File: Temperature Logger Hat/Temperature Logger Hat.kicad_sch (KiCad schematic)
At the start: 18 parts, among them J1 GPIO, J2 SPI, J3 1-wire, J4 Jumper_Mode, SW1 SW_Power_Off, SW2 SW_Mode2, U1 CAT24C256

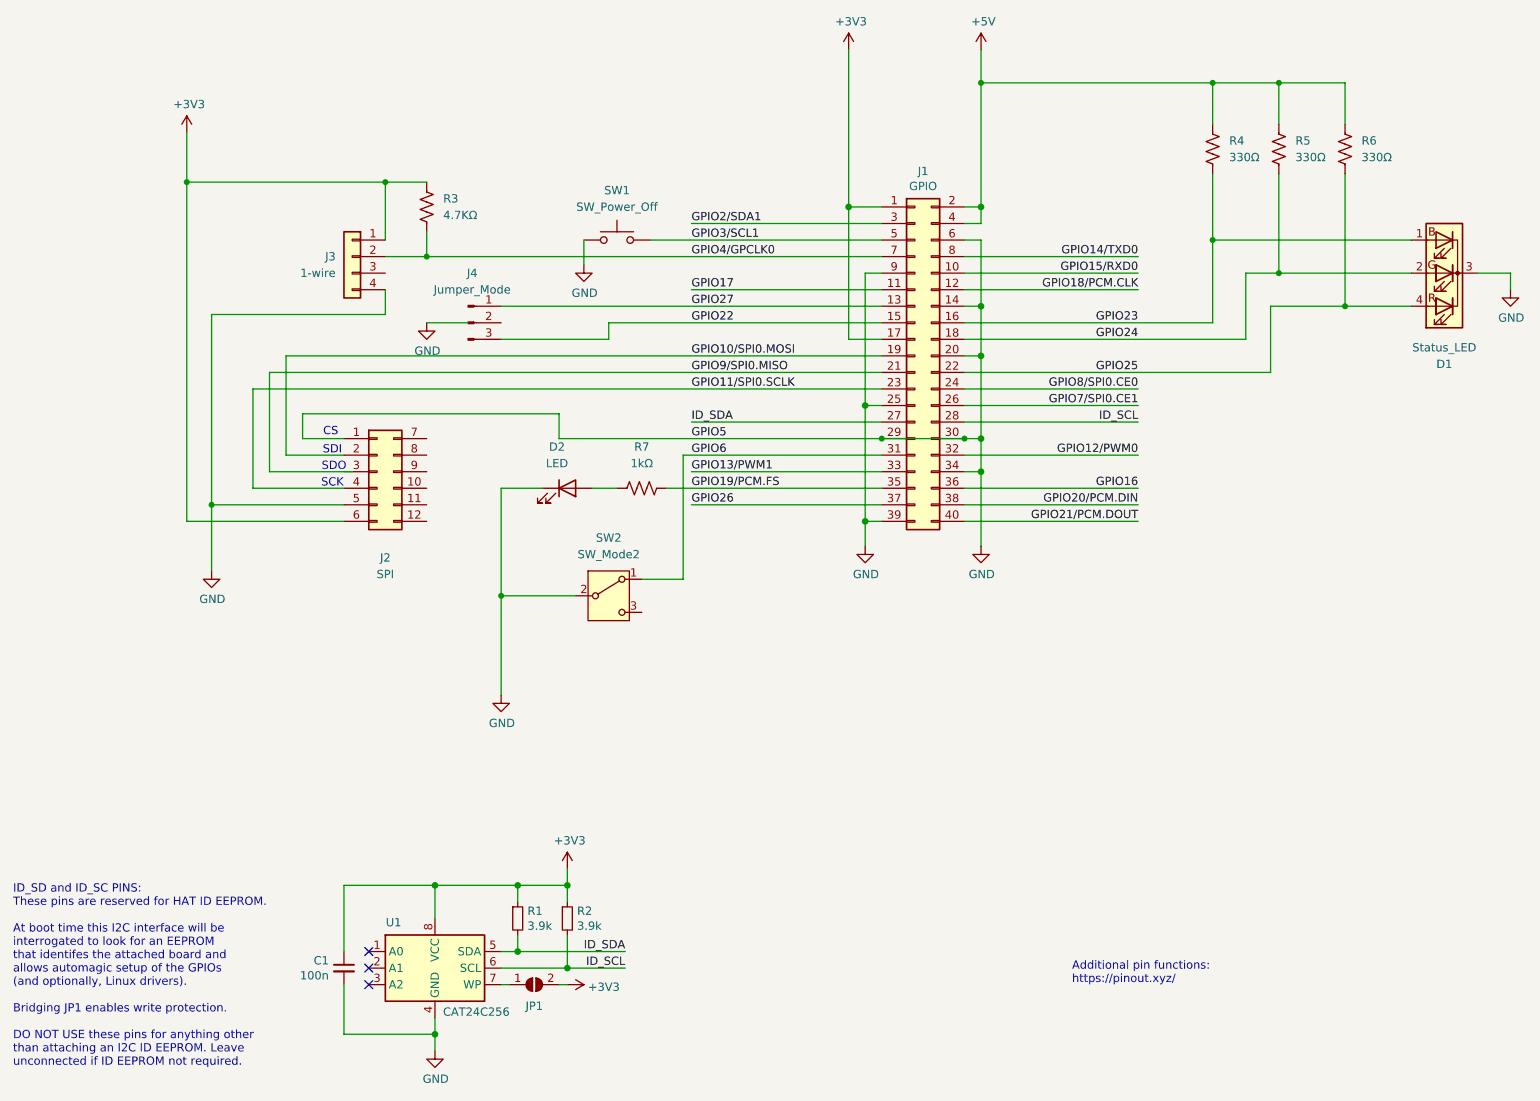
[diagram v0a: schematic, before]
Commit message: Documentation and test update (#14)
* Fix LED connections in schematic

* Add 'zeropi' to host inventory

* Fix installation documentation

* Add standalone script to test SPI Temperature sensor

* Update schematic for Hat

* Remove superfluous init code

* Add resistance to test report
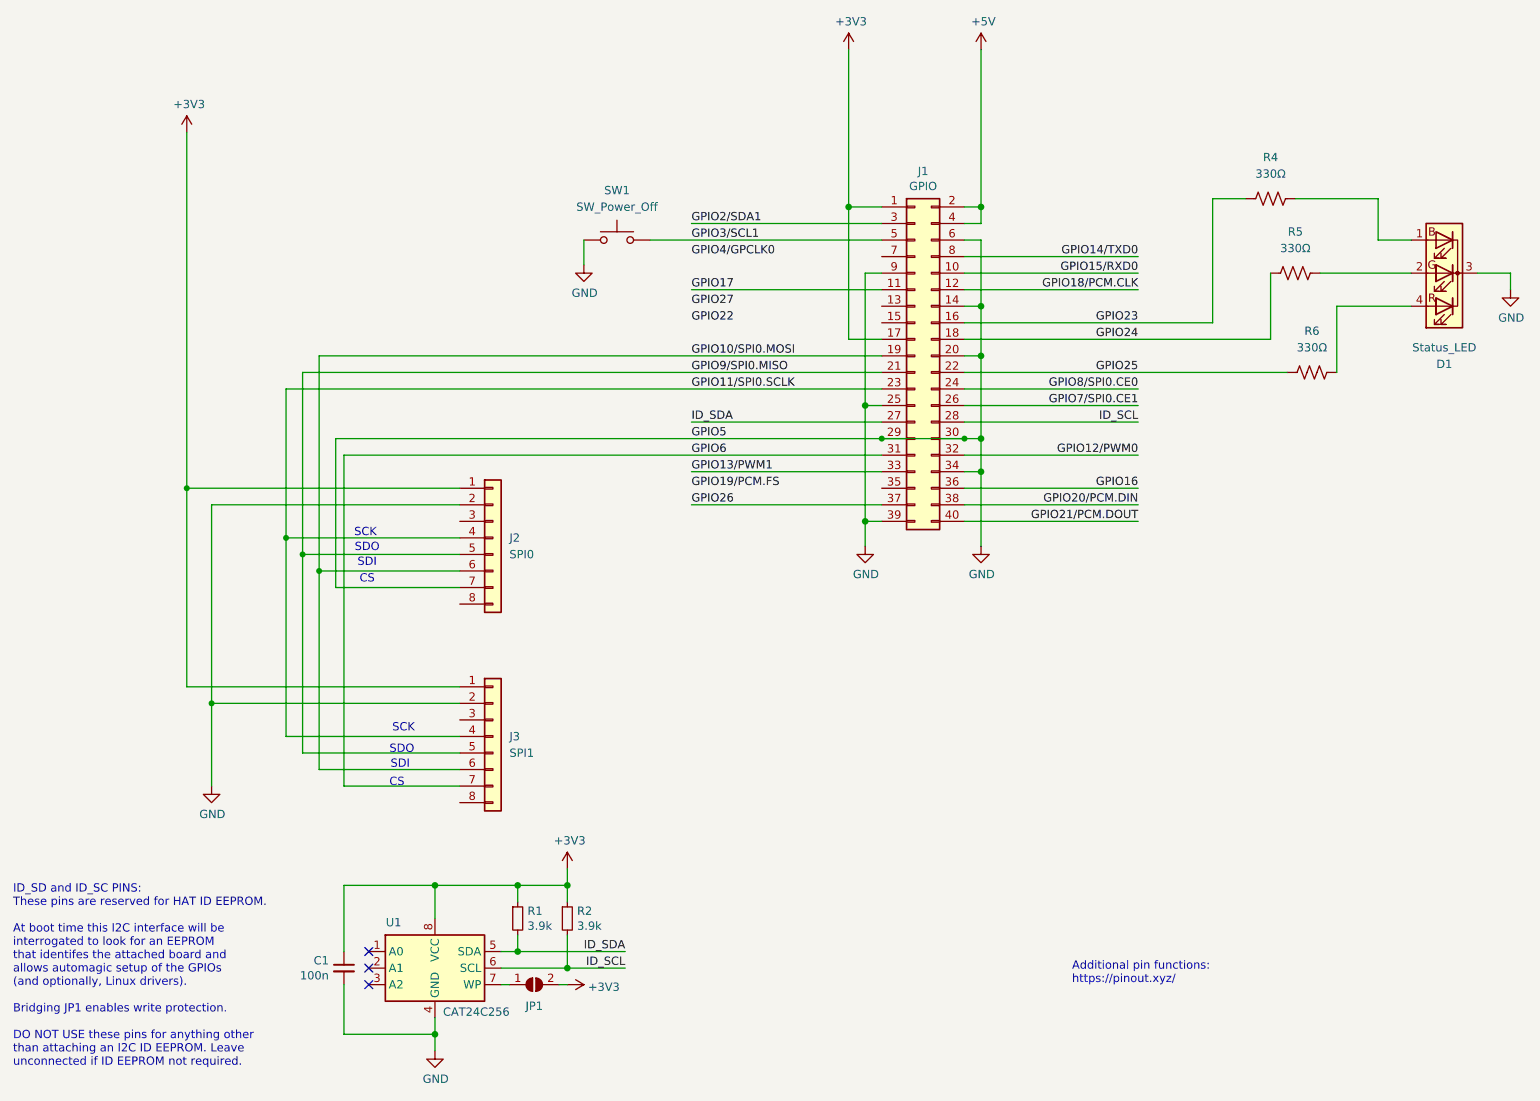
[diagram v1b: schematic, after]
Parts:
- removed D2: LED, symbol Device:LED
- removed J2: SPI, symbol Connector_Generic:Conn_02x06_Top_Bottom
- removed J3: 1-wire, symbol Connector_Generic:Conn_01x04
- removed J4: Jumper_Mode, symbol Connector:Conn_01x03_Pin
- removed R3: 4.7KΩ, symbol Device:R_US
- removed R7: 1kΩ, symbol Device:R_US
- removed SW2: SW_Mode2, symbol Switch:SW_SPDT
- added J2: SPI0, symbol Connector_Generic:Conn_01x08
- added J3: SPI1, symbol Connector_Generic:Conn_01x08
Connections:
- net +3V3: now also J2.1 (Pin_1), J3.1 (Pin_1)
- net +5V: no longer R4.1, R5.1, R6.1
- net GND: now also J2.2 (Pin_2), J2.7 (Pin_7), J3.2 (Pin_2)
- net GPIO10/SPI0.MOSI: now also J2.6 (Pin_6), J3.6 (Pin_6)
- net GPIO11/SPI0.SCLK: now also J2.4 (Pin_4), J3.4 (Pin_4)
- net GPIO19/PCM.FS: no longer J1.35 (Pin_35)
- net GPIO22: no longer J1.15 (Pin_15)
- net GPIO23: no longer D1.1 (BA)
- net GPIO24: no longer D1.2 (GA)
- net GPIO25: no longer D1.4 (RA)
- net GPIO27: no longer J1.13 (Pin_13)
- net GPIO4/GPCLK0: no longer J1.7 (Pin_7)
- net GPIO6: now also J3.7 (Pin_7)
- net GPIO9/SPI0.MISO: now also J2.5 (Pin_5), J3.5 (Pin_5)
- new net: D1.4 (RA), R6.1
- new net: D1.1 (BA), R4.1
- new net: D1.2 (GA), R5.1
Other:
- moved on the sheet: R4, R5, R6
